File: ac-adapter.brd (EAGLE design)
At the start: 63 parts, among them IC1 SSC3S900, IC2 TL431, Q1 300V5A, Q2 300V5A, Q3 TLP621-1, T1 COMMON_FILTER-SU10VFC, T2 TRANSFORMAER_FLYBACK-PQ2620

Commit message: 完成
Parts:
- added DR1, DR2, DR3, DR4: HOLE-3.2, my_connector:HOLE_3.2
- D4: device my_rcl:KBJ410 -> my_rcl:RBA-406
- moved TP3 73.3 mm to (80.0, 59.7)
- moved TP5 72.7 mm to (74.3, 59.7)
- moved TP4 71.6 mm to (69.8, 59.7)
- moved C22 66.8 mm to (66.7, 52.1), turned to 180 degrees
- moved C21 63.9 mm to (76.8, 52.1), turned to 180 degrees
- moved L1 58.1 mm to (77.5, 42.5), turned to 270 degrees
- moved L2 54.2 mm to (68.6, 42.5), turned to 270 degrees
- moved C18 47.6 mm to (69.8, 31.8)
- moved C17 47.3 mm to (69.8, 19.1)
- moved R1 43.2 mm to (17.5, 24.1)
- moved Q1 42.8 mm to (24.1, 24.1)
- moved Q2 42.8 mm to (24.1, 34.3)
- moved C2 42.8 mm to (11.4, 39.4)
- moved C3 42.8 mm to (29.2, 34.3)
- moved C7 42.8 mm to (9.53, 8.89)
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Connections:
- removed net N$26: C17.+, C19.2, D4.1, L1.2
- new net N$40: C17.+, D4.1, L1.2, R13.1, R16.2, R17.1
- net N$35: now also C19.2, T2.7; no longer R13.1
- net N$36: now also T2.12
- net V+: no longer R16.2, R17.1
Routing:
- net PGND: track 189.4 -> 111.2 mm, vias 0 -> 23
- net N$40: track 0.00 -> 57.8 mm
- net V+: track 65.1 -> 15.7 mm
- net GND: track 129.9 -> 85.4 mm, vias 0 -> 8
- net N$36: track 15.3 -> 38.4 mm
- net N$26: track 19.6 -> 0.00 mm
- net N$35: track 15.3 -> 29.0 mm
- net V-: track 14.8 -> 18.9 mm
- net N$19: track 41.5 -> 38.6 mm
- net N$22: track 23.4 -> 25.8 mm
- net VH: track 89.0 -> 91.2 mm
- net N$17: track 6.45 -> 5.13 mm
- net N$7: track 20.4 -> 19.4 mm
- net N$27: track 23.1 -> 24.0 mm
- net N$9: track 10.8 -> 11.7 mm
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- added copper zone on layer 1, net GND
- added copper zone on layer 16, net GND
- added copper zone on layer 16, net N$35
- added copper zone on layer 16, net N$36
- added copper zone on layer 1, net N$40
- added copper zone on layer 16, net N$7
- added copper zone on layer 16, net N$8
- added copper zone on layer 1, net PGND
- added copper zone on layer 16, net PGND
- added copper zone on layer 16, net SW
- added copper zone on layer 16, net V+
- added copper zone on layer 16, net V-
- added copper zone on layer 1, net VH
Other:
- board outline added: 85.1 x 72.4 mm

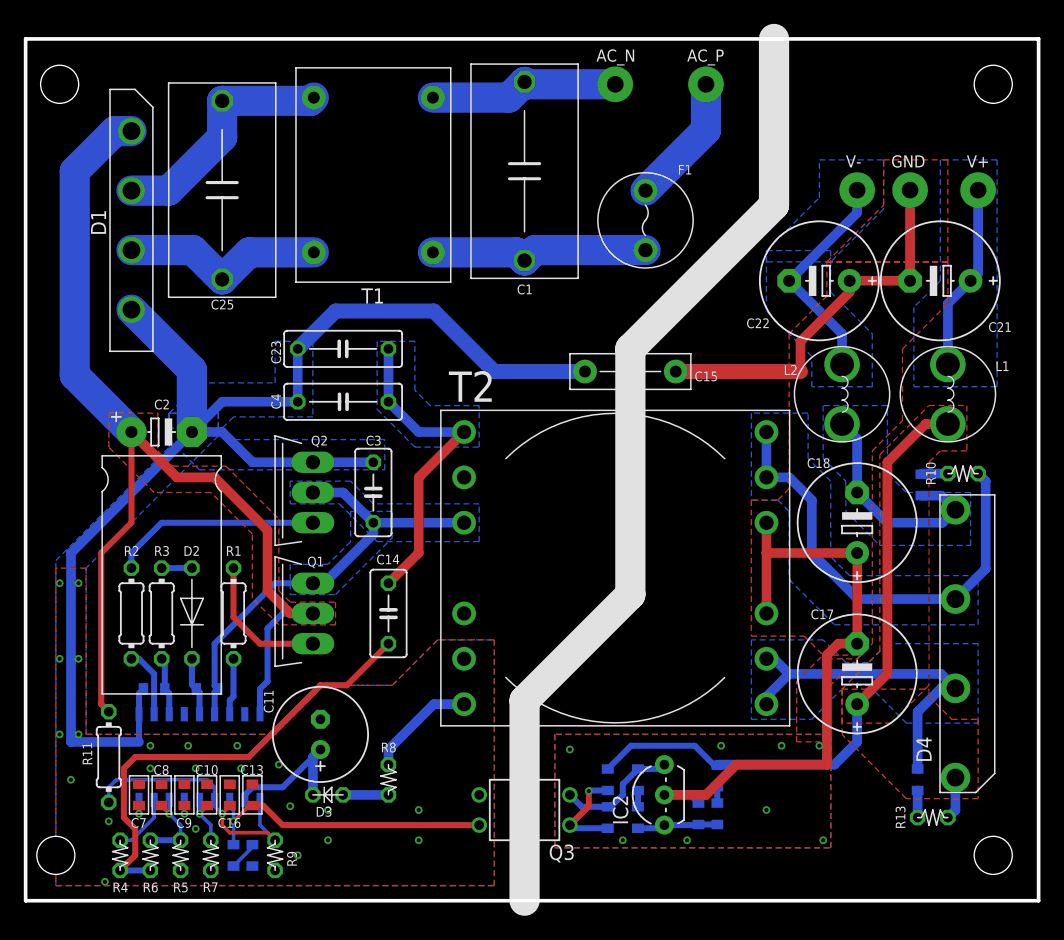
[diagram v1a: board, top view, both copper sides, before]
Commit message: 電解コン大きく
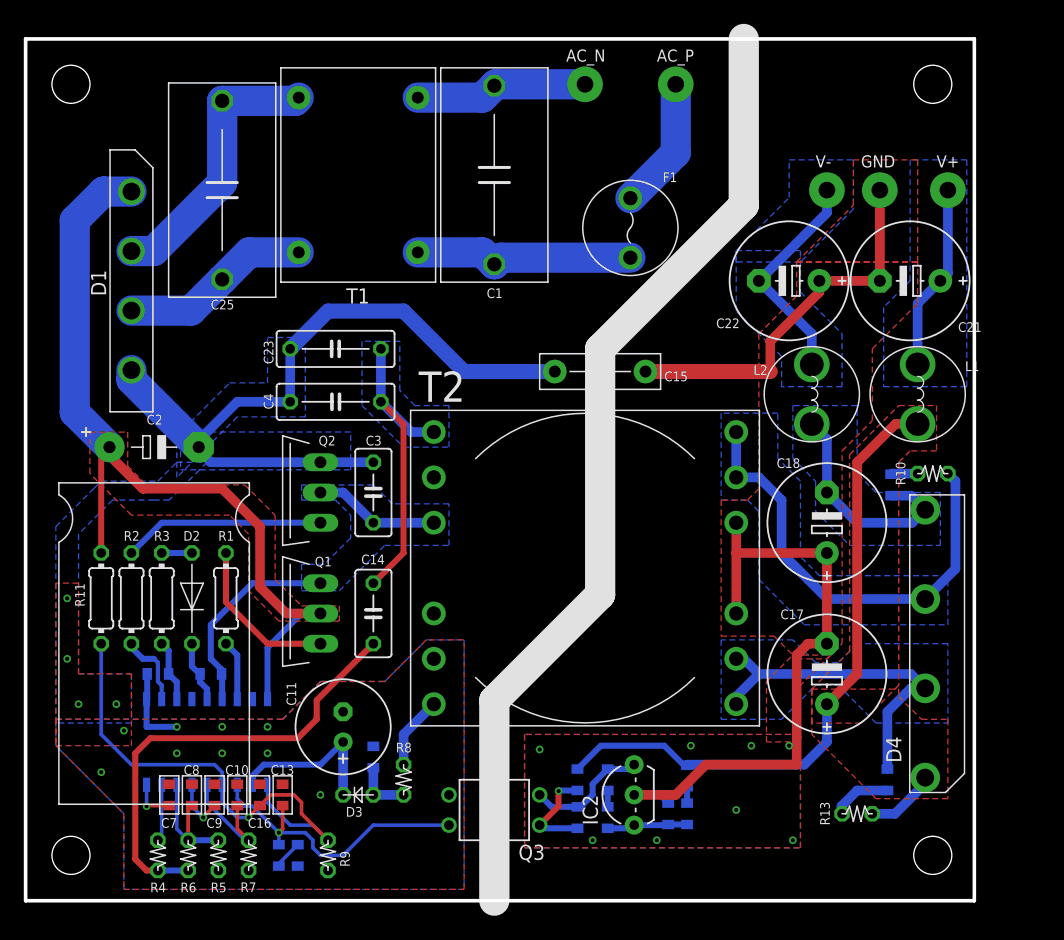
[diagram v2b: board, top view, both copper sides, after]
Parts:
- added C26: 1000p, my_rcl:1608
- C2: device my_rcl:E5-10,5A -> my_rcl:E5-16A
- moved R11 13.4 mm to (6.35, 25.4)
- moved R13 6.36 mm to (69.8, 7.30)
- moved D1 5.08 mm to (8.89, 52.1)
- moved DR3 5.08 mm to (76.2, 3.81)
- moved DR4 5.08 mm to (76.2, 68.6)
- moved R9 4.45 mm to (25.4, 3.81)
- moved R12 3.81 mm to (21.3, 3.81)
- moved C12 3.81 mm to (22.9, 3.81)
- moved R7 3.18 mm to (18.7, 3.81)
- moved R4 3.18 mm to (11.1, 3.81)
- moved R6 3.18 mm to (13.7, 3.81)
- moved R5 3.17 mm to (16.2, 3.81)
- moved C1 2.56 mm to (39.4, 61.0)
- moved C19 2.54 mm to (72.4, 10.2)
- moved C20 2.54 mm to (72.7, 34.9)
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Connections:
- net N$25: now also C26.1
- net PGND: now also C26.2
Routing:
- net PGND: track 111.2 -> 70.9 mm, vias 23 -> 13
- net VH: track 91.2 -> 71.4 mm
- net N$27: track 24.0 -> 41.9 mm
- net SW: track 38.0 -> 28.2 mm
- net N$21: track 4.73 -> 9.59 mm, vias 1 -> 0
- net N$18: track 7.27 -> 10.6 mm, vias 1 -> 0
- net N$5: track 20.3 -> 23.4 mm
- net N$24: track 9.20 -> 6.13 mm
- net N$3: track 2.27 -> 5.07 mm
- net N$20: track 1.85 -> 4.54 mm
- net N$40: track 57.8 -> 60.2 mm
- net N$16: track 1.85 -> 3.72 mm
- net N$9: track 11.7 -> 13.5 mm
- net N$23: track 12.4 -> 14.0 mm
- net AC_N: track 15.9 -> 14.5 mm
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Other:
- board size 85.1 x 72.4 mm -> 79.7 x 72.4 mm

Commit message: 微修正
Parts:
- moved DR4 1.80 mm to (77.5, 69.8)
- moved C18 1.27 mm to (67.3, 33.0)
- moved C20 1.27 mm to (72.7, 36.2)
- moved C21 1.27 mm to (74.3, 53.3)
- moved C22 1.27 mm to (64.1, 53.3)
- moved C23 1.27 mm to (26.0, 47.6)
- moved C25 1.27 mm to (16.5, 61.0)
- moved C3 1.27 mm to (29.2, 35.6)
- moved C4 1.27 mm to (26.0, 43.2)
- moved D1 1.27 mm to (8.89, 53.3)
- moved D2 1.27 mm to (14.0, 26.7)
- moved Q2 1.27 mm to (24.8, 35.6)
- moved R1 1.27 mm to (16.8, 26.7)
- moved R10 1.27 mm to (76.2, 37.1)
- moved R11 1.27 mm to (6.35, 26.7)
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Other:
- board size 79.7 x 72.4 mm -> 81.3 x 73.7 mm
- board text added: "LLC AC adapter ±20V 3A"

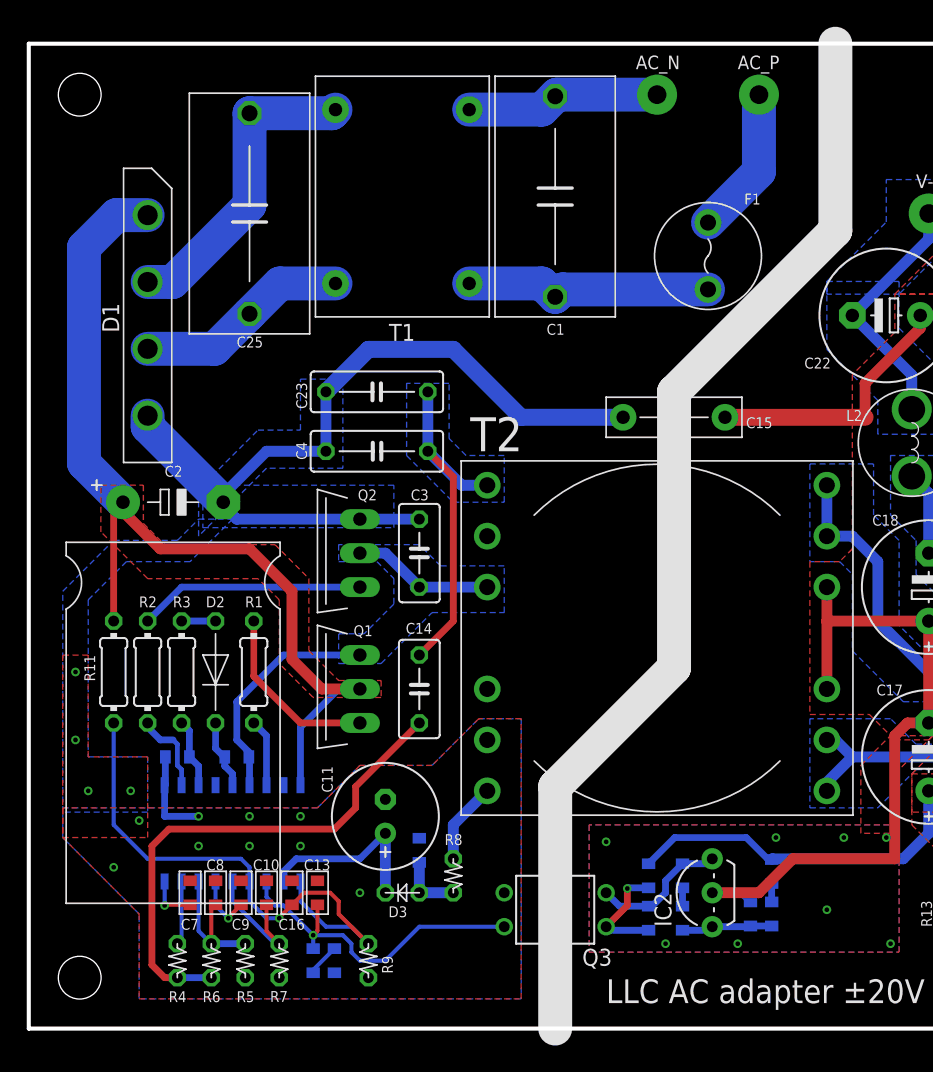
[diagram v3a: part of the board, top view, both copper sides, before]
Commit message: コモンモードフィルタ追加
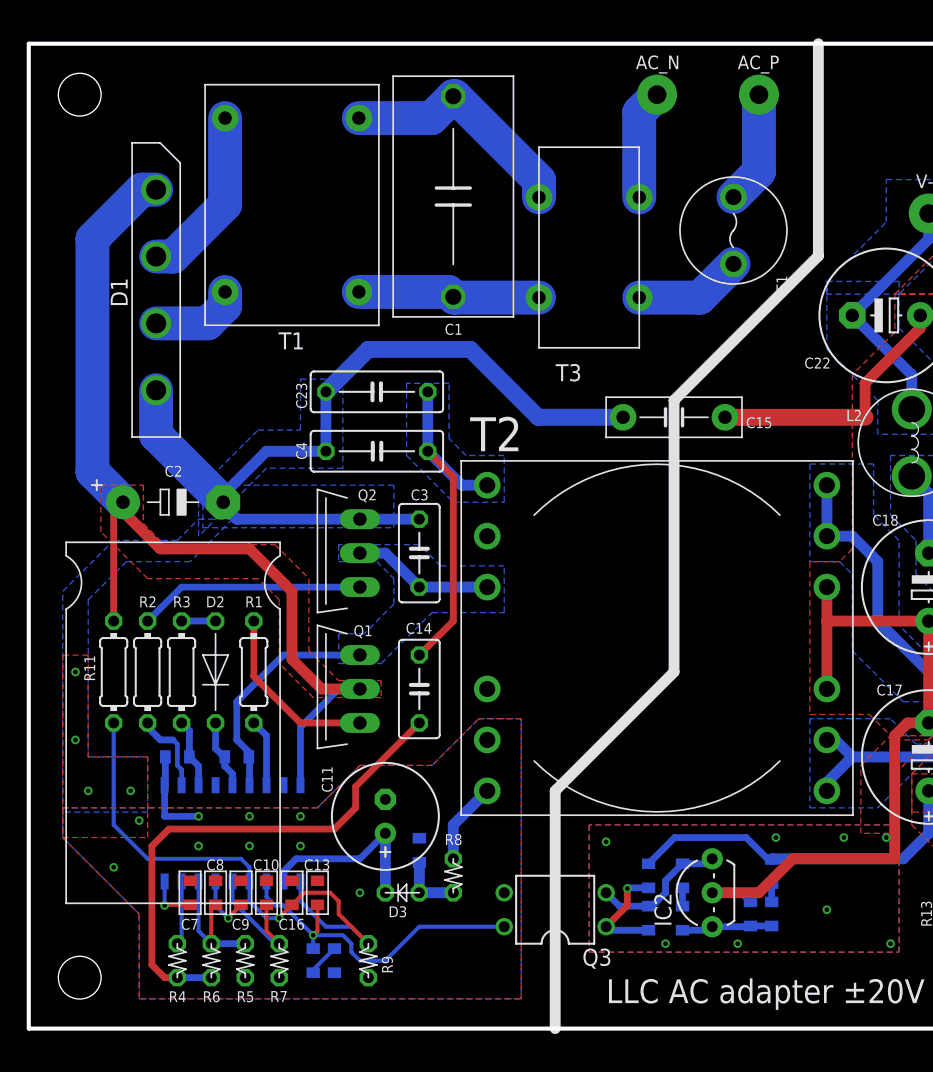
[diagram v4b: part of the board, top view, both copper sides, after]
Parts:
- removed C25: 0.22uX, my_rcl:X-CAPACITER
- added T3: COMMON_FILTER-SMALL, my_rcl:COMMON_FILTER__SMALL
- F1: value 250V1A -> 2A250V
- moved T1 8.28 mm to (19.7, 61.6)
- moved C1 7.62 mm to (31.8, 62.2)
- moved F1 2.69 mm to (52.7, 59.7)
- moved D1 2.01 mm to (9.53, 55.2)
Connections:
- net AC_P renamed N$37
- removed net AC_N: C1.2, T1.3, TP2.1
- new net N$26: C1.2, T1.3, T3.2
- new net N$30: T3.1, TP2.1
- new net N$31: F1.2, T3.4
- net N$1: now also T3.3; no longer F1.2
- net N$4: no longer C25.1
- net N$5: no longer C25.2
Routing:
- net N$26: track 0.00 -> 18.0 mm
- net AC_N: track 14.5 -> 0.00 mm
- net N$5: track 23.4 -> 13.2 mm
- net N$4: track 16.1 -> 6.74 mm
- net N$30: track 0.00 -> 8.23 mm
- net N$31: track 0.00 -> 8.09 mm
- net N$1: track 18.5 -> 13.7 mm
- net N$37: track 11.1 -> 8.45 mm
- net PGND: track 70.9 -> 72.5 mm
- net VH: track 71.4 -> 72.3 mm

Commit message: 微修正
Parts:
- added R20, R21: 10k, my_rcl:1608
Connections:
- removed net N$11: Q2.1, R2.1
- removed net N$9: Q1.1, R1.1
- new net N$38: Q1.1, R1.1, R20.2
- new net N$39: Q2.1, R2.1, R21.1
- net PGND: now also R21.2
- net SW: now also R20.1
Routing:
- net N$39: track 0.00 -> 17.2 mm
- net N$11: track 16.9 -> 0.00 mm
- net N$38: track 0.00 -> 16.5 mm
- net N$9: track 13.5 -> 0.00 mm
- net PGND: track 72.5 -> 75.4 mm
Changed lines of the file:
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@@
 <attribute name="VALUE" x="48.705" y="56.84" size="0.8128" layer="27" font="vector" rot="R270"/>
+</element>
+<element name="R20" library="my_rcl" package="1608" value="10k" x="19.685" y="29.21" smashed="yes" rot="MR90">
+<attribute name="NAME" x="20.685" y="27.61" size="0.8128" layer="26" rot="MR90"/>
+<attribute name="VALUE" x="17.885" y="27.61" size="0.8128" layer="28" rot="MR90"/>
+</element>
+<element name="R21" library="my_rcl" package="1608" value="10k" x="20.32" y="34.29" smashed="yes" rot="MR90">
+<attribute name="NAME" x="21.32" y="32.69" size="0.8128" layer="26" rot="MR90"/>
+<attribute name="VALUE" x="18.52" y="32.69" size="0.8128" layer="28" rot="MR90"/>
 </element>
 </elements>
@@
 <wire x1="15.5575" y1="21.59" x2="15.5575" y2="24.4475" width="0.508" layer="16"/>
 <wire x1="15.5575" y1="24.4475" x2="19.05" y2="27.94" width="0.508" layer="16"/>
-<wire x1="19.05" y1="27.94" x2="24.765" y2="27.94" width="0.508" layer="16"/>
+<wire x1="19.05" y1="27.94" x2="19.685" y2="27.94" width="0.508" layer="16"/>
+<wire x1="19.685" y1="27.94" x2="24.765" y2="27.94" width="0.508" layer="16"/>
 <wire x1="16.4575" y1="20.69" x2="15.5575" y2="21.59" width="0.508" layer="16"/>
-</signal>
-<signal name="N$9">
-<contactref element="Q1" pad="1"/>
-<contactref element="R1" pad="1"/>
-<wire x1="24.765" y1="22.86" x2="20.32" y2="22.86" width="0.508" layer="1"/>
-<wire x1="20.32" y1="22.86" x2="16.8275" y2="26.3525" width="0.508" layer="1"/>
-<wire x1="16.8275" y1="26.3525" x2="16.8275" y2="30.48" width="0.508" layer="1"/>
-</signal>
-<signal name="N$11">
-<contactref element="R2" pad="1"/>
-<contactref element="Q2" pad="1"/>
-<wire x1="24.765" y1="33.02" x2="11.43" y2="33.02" width="0.508" layer="16"/>
-<wire x1="8.89" y1="30.48" x2="11.43" y2="33.02" width="0.508" layer="16"/>
+<contactref element="R20" pad="1"/>
+<wire x1="19.685" y1="28.31" x2="19.685" y2="27.94" width="0.508" layer="16"/>
 </signal>
 <signal name="N$12">
@@
 <wire x1="15.5575" y1="38.1" x2="14.605" y2="39.0525" width="0.8128" layer="16"/>
 <wire x1="14.545" y1="39.37" x2="14.605" y2="39.37" width="0.8128" layer="16"/>
-<wire x1="15.5575" y1="38.1" x2="24.765" y2="38.1" width="0.8128" layer="16"/>
+<wire x1="15.5575" y1="38.1" x2="20.32" y2="38.1" width="0.8128" layer="16"/>
+<wire x1="20.32" y1="38.1" x2="24.765" y2="38.1" width="0.8128" layer="16"/>
 <wire x1="24.765" y1="38.1" x2="29.21" y2="38.1" width="0.8128" layer="16"/>
 <contactref element="C23" pad="2"/>
@@
 <wire x1="10.16" y1="18.205" x2="10.16" y2="15.875" width="0.508" layer="16"/>
 <wire x1="10.16" y1="15.875" x2="12.7" y2="15.875" width="0.508" layer="16"/>
+<contactref element="R21" pad="2"/>
+<wire x1="20.32" y1="38.1" x2="20.32" y2="35.19" width="0.508" layer="16"/>
 </signal>
 <signal name="N$2">
@@
 <wire x1="54.61" y1="64.095" x2="52.705" y2="62.19" width="2.54" layer="16"/>
 </signal>
+<signal name="N$38">
+<contactref element="R20" pad="2"/>
+<contactref element="Q1" pad="1"/>
+<contactref element="R1" pad="1"/>
+<wire x1="24.765" y1="22.86" x2="20.32" y2="22.86" width="0.508" layer="1"/>
+<wire x1="20.32" y1="22.86" x2="16.8275" y2="26.3525" width="0.508" layer="1"/>
+<wire x1="16.8275" y1="26.3525" x2="16.8275" y2="30.48" width="0.508" layer="1"/>
+<wire x1="19.685" y1="30.11" x2="17.1975" y2="30.11" width="0.508" layer="16"/>
+<wire x1="17.1975" y1="30.11" x2="16.8275" y2="30.48" width="0.508" layer="16"/>
+</signal>
+<signal name="N$39">
+<contactref element="R21" pad="1"/>
+<contactref element="R2" pad="1"/>
+<contactref element="Q2" pad="1"/>
+<wire x1="11.43" y1="33.02" x2="8.89" y2="30.48" width="0.508" layer="16"/>
+<wire x1="24.765" y1="33.02" x2="20.69" y2="33.02" width="0.508" layer="16"/>
+<wire x1="20.69" y1="33.02" x2="20.32" y2="33.39" width="0.508" layer="16"/>
+<wire x1="20.32" y1="33.39" x2="19.95" y2="33.02" width="0.508" layer="16"/>
+<wire x1="19.95" y1="33.02" x2="11.43" y2="33.02" width="0.508" layer="16"/>
+</signal>
 </signals>

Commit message: 消した
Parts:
- removed C10, C6: 1u, my_rcl:1608
- removed C11: 35V100uF, my_rcl:E2,5-8
- removed C12, C9: 0.22u, my_rcl:1608
- removed C13, C16, C26: 1000p, my_rcl:1608
- removed C14: 100pF1kV, my_rcl:C050
- removed C3: 470pF1kV, my_rcl:C050
- removed C4: 400V0.01uF, my_rcl:C100
- removed C5: 0.1u, my_rcl:1608
- removed C7: 3300p, my_rcl:1608
- removed C8: 100p, my_rcl:1608
- removed D2: 500V 0.1A, my_rcl:D0204/7
- removed D3: 0.1A, my_rcl:D0207/2V
- removed IC1: SSC3S900, my_ic:SOP18
- removed R11: 1M, my_rcl:0204/7
- removed R12: 10k, my_rcl:1608
- removed R3: 4.7, my_rcl:0204/7
- removed R4: 100k, my_rcl:0207/2V
- removed R5, R6: 47, my_rcl:0207/2V
- removed R7: fmin, my_rcl:0207/2V
- removed R8: 10, my_rcl:0207/2V
- removed R9: 22k, my_rcl:0207/2V
- added L3: (no value), my_rcl:BPQ20/20
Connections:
- removed net N$12: IC1.11, R2.2
- removed net N$13: C6.1, IC1.12, R3.1
- removed net N$14: IC1.16, R1.2
- removed net N$15: C5.2, D2.2, IC1.14
- removed net N$16: C7.1, IC1.9
- removed net N$17: IC1.8, R4.2
- removed net N$18: C8.1, IC1.7, R5.1, R6.2
- removed net N$19: C14.2, R4.1, R6.1
- removed net N$20: C9.2, IC1.6
- removed net N$21: C10.2, IC1.5, R7.2
- removed net N$23: C11.+, D3.2, IC1.2
- removed net N$24: R8.2, T2.6
- removed net N$25: C26.1, D3.1, R8.1
- removed net N$27: C16.1, IC1.1, IC1.4, R11.2, R9.1
- removed net N$28: C12.1, R12.1
- removed net N$38: Q1.1, R1.1, R20.2
- removed net N$39: Q2.1, R2.1, R21.1
- removed net PGND: C10.1, C11.-, C12.2, C13.2, C15.2, C16.2, C2.-, C23.2, C26.2, C3.2, C4.1, C6.2, C7.2, C8.2, C9.1, D1.4, IC1.10, Q2.3, Q3.3, R21.2, R5.2, R7.1, R9.2, T2.5
- new net N$11: L3.4, L3.5, L3.6, T2.1
- new net N$43: Q3.3
- new net N$44: C2.-, C23.2, D1.4, Q2.3, R21.1
- new net N$9: Q2.1, R2.1, R21.2
- net N$2: now also Q1.1, R1.1, R20.1; no longer D2.1, R3.2
- net N$22: no longer C13.1, IC1.3, R12.2
- net N$8: now also T2.3; no longer C14.1, C4.2, T2.1
- net SW: now also L3.1, L3.2, L3.3, R20.2; no longer C3.1, C5.1, IC1.15, R20.1, T2.3
- net VH: no longer IC1.18, R11.1
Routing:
- net GND: track 85.4 -> 0.00 mm, vias 8 -> 0
- net PGND: track 75.4 -> 0.00 mm, vias 13 -> 0
- net VH: track 72.3 -> 0.00 mm
- net N$40: track 60.2 -> 0.00 mm
- net N$27: track 41.9 -> 0.00 mm, vias 1 -> 0
- net N$19: track 38.5 -> 0.00 mm
- net N$36: track 38.4 -> 0.00 mm
- net N$35: track 29.0 -> 0.00 mm
- net SW: track 28.6 -> 0.00 mm
- net N$8: track 27.0 -> 0.00 mm
- net N$22: track 25.8 -> 0.00 mm, vias 1 -> 0
- net N$7: track 19.4 -> 0.00 mm
- net V-: track 18.9 -> 0.00 mm
- net N$26: track 18.0 -> 0.00 mm
- net N$39: track 17.2 -> 0.00 mm
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- removed copper zone on layer 1, net GND
- removed copper zone on layer 16, net GND
- removed copper zone on layer 16, net N$35
- removed copper zone on layer 16, net N$36
- removed copper zone on layer 1, net N$40
- removed copper zone on layer 16, net N$7
- removed copper zone on layer 16, net N$8
- removed copper zone on layer 1, net PGND
- removed copper zone on layer 16, net PGND
- removed copper zone on layer 16, net SW
- removed copper zone on layer 16, net V+
- removed copper zone on layer 16, net V-
- removed copper zone on layer 1, net VH
